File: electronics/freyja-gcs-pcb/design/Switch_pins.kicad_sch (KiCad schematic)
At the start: 21 parts, among them SW3 TS1210CJ 250GF 009, U3 ST-0-102-A01-T000-LF+PJ, U4 ST-0-102-A01-T000-LF+PJ, U5 ST-0-102-A01-T000-LF+PJ, U6 ST-0-102-A01-T000-LF+PJ, U7 ST-0-102-A01-T000-LF+PJ, U8 ST-0-102-A01-T000-LF+PJ

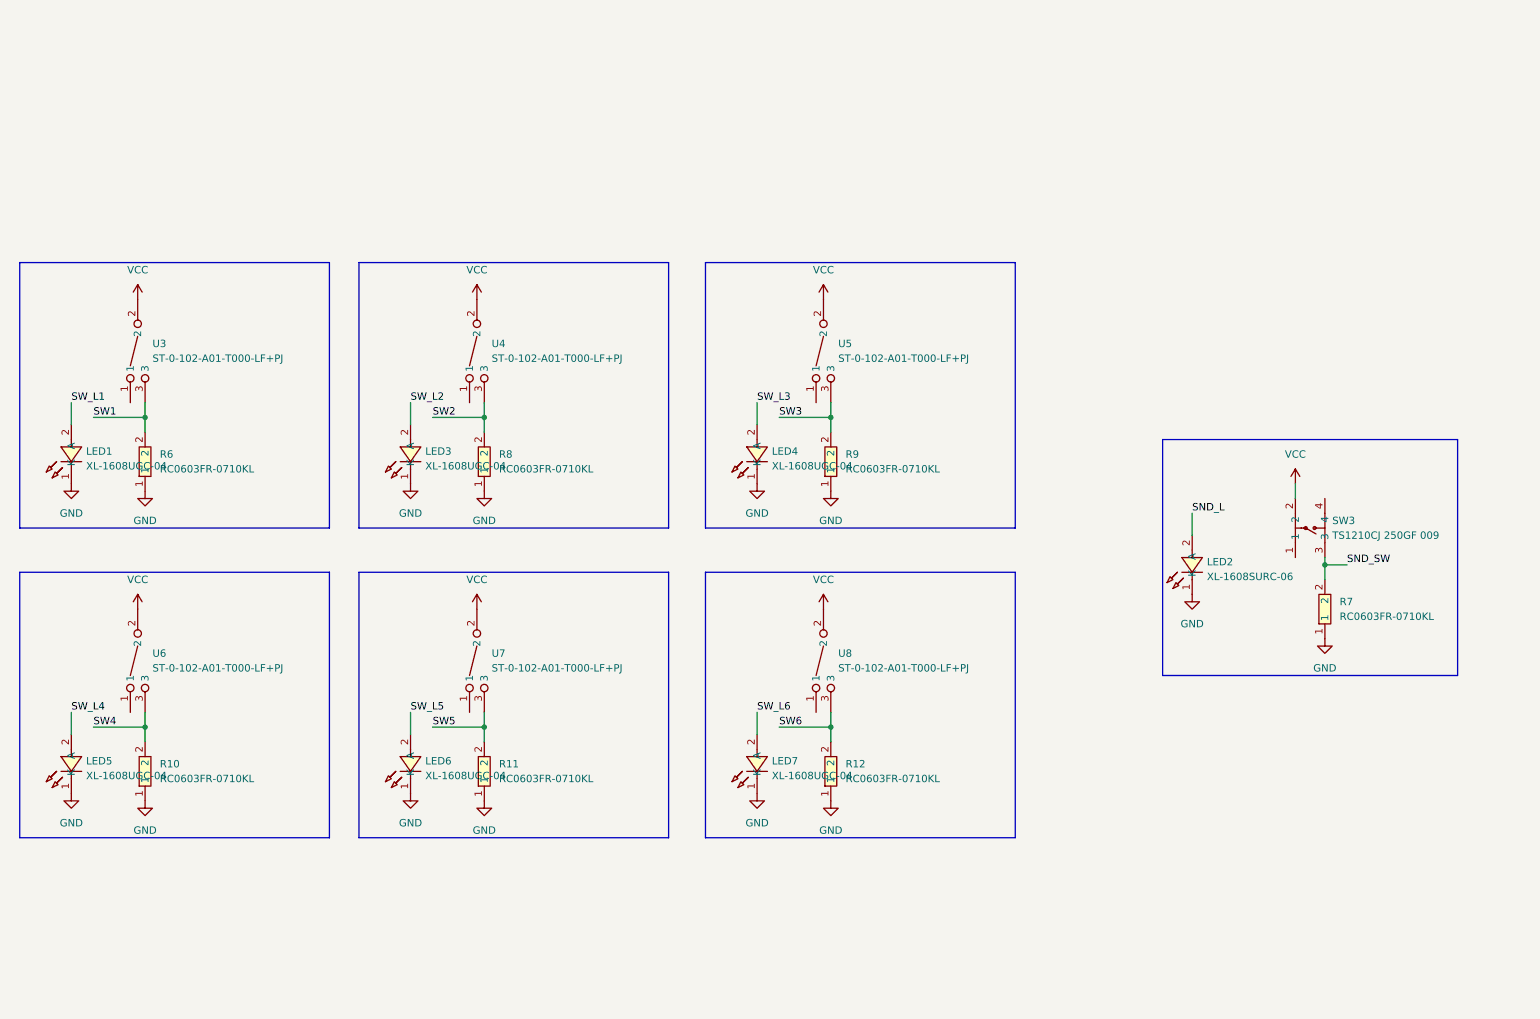
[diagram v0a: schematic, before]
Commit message: reset annotation
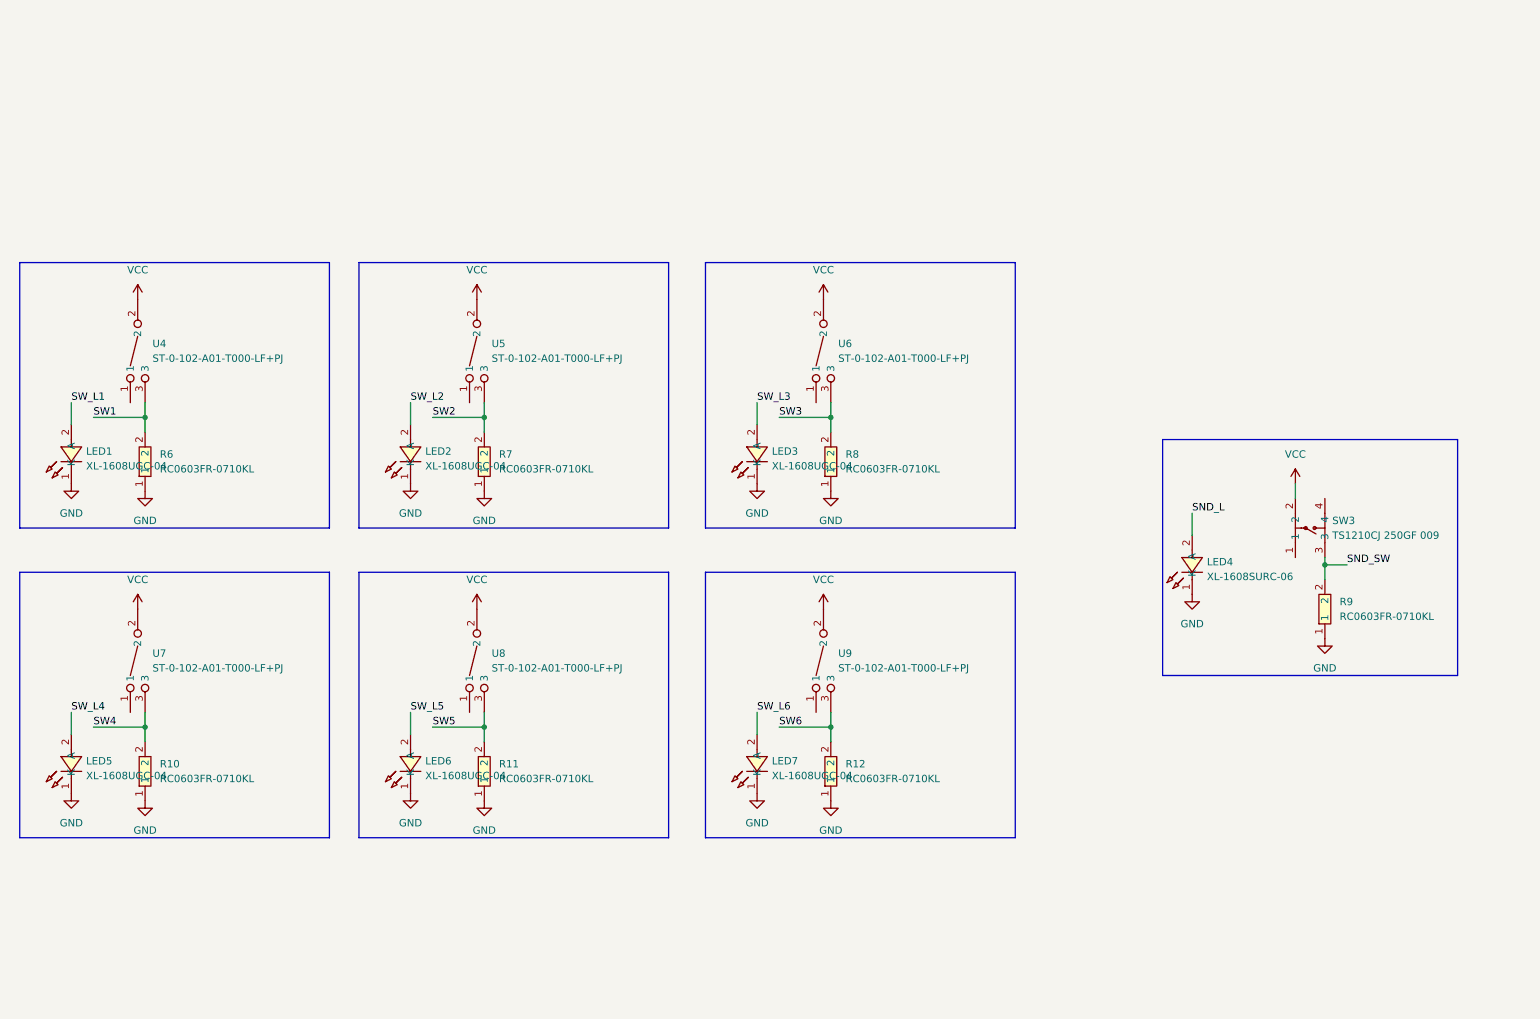
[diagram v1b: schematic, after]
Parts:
- renumbered LED3 to LED2, LED4 to LED3, LED2 to LED4, R8 to R7, R9 to R8, R7 to R9, U3 to U4, U4 to U5, U5 to U6, U6 to U7, U7 to U8, U8 to U9

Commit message: add led backlight driver
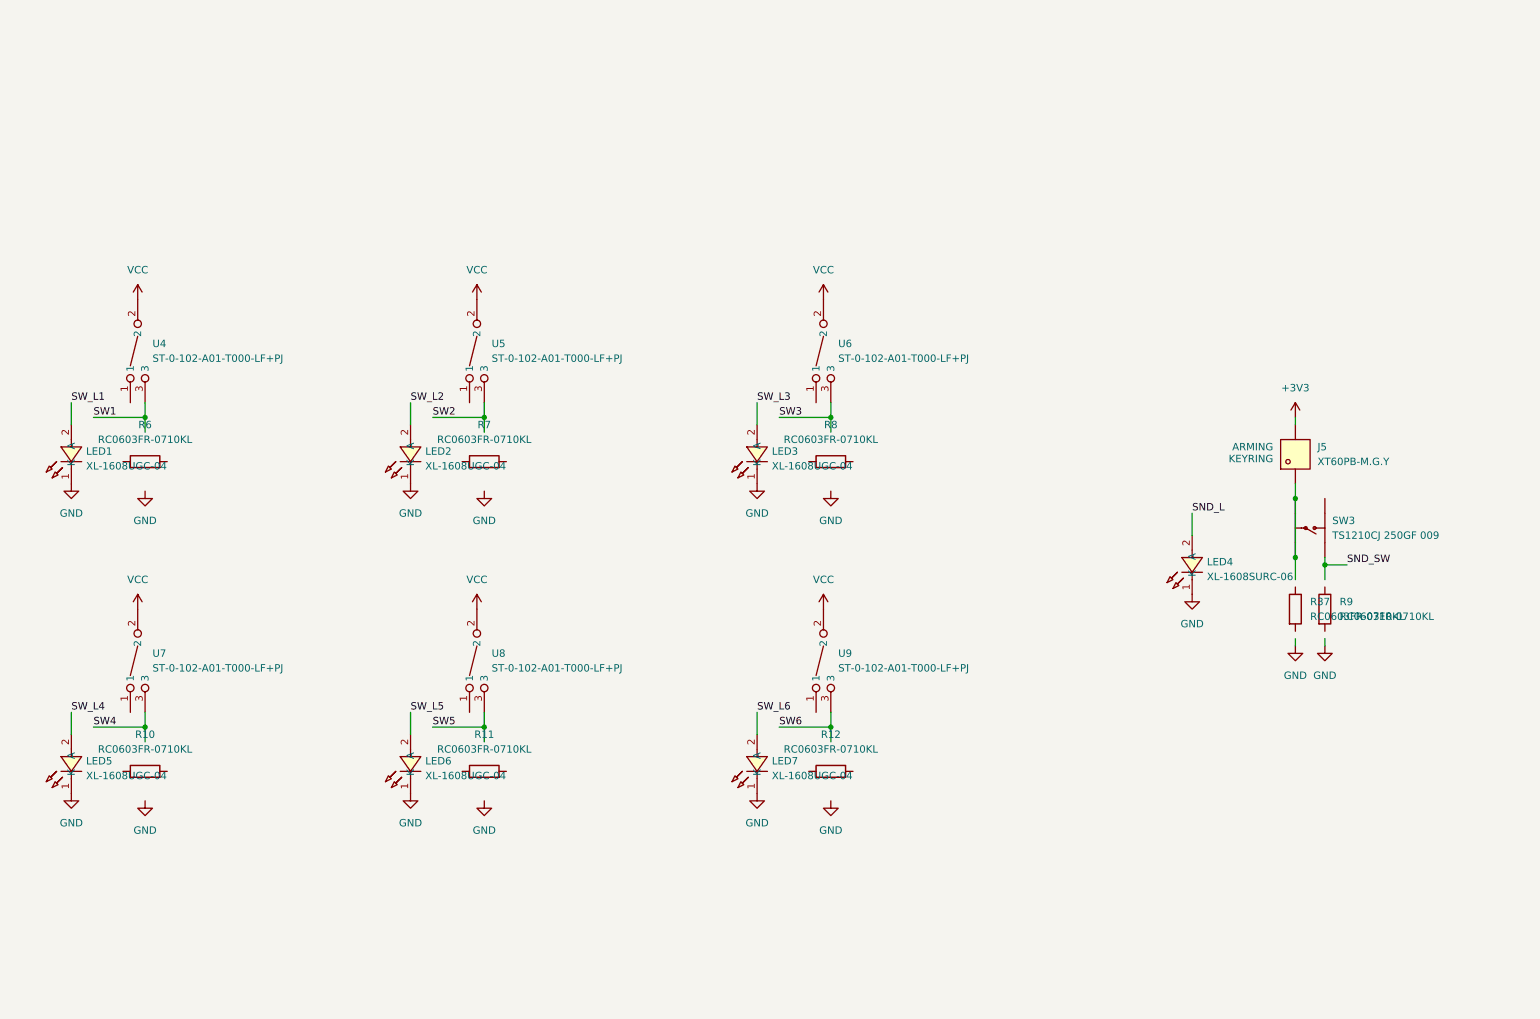
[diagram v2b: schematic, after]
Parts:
- added J5: XT60PB-M.G.Y, EasyEDA:CONN-TH_XT60PB-M, symbol EasyEDA:XT60PB-M.G.Y
- added R37: RC0603FR-0710KL, EasyEDA:R0603, symbol Device:R
- R10, R11, R12, R6, R7, R8, R9: symbol EasyEDA:RC0603FR-0710KL -> Device:R
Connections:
- net GND: no longer R10.1, R11.1, R12.1, R6.1, R7.1, R8.1, R9.1
- net SND_SW: no longer R9.2
- net SW1: no longer R6.2
- net SW2: no longer R7.2
- net SW3: no longer R8.2
- net SW4: no longer R10.2
- net SW5: no longer R11.2
- net SW6: no longer R12.2
- net VCC: no longer SW3.2
- net at SW3.1: now also SW3.2, J5.1
- new net +3V3: J5.2
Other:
- note added: "ARMING KEYRING"

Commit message: buttons and indicators
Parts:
- removed LED1, LED2, LED3, LED5, LED6, LED7: XL-1608UGC-04, EasyEDA:LED0603-RD_GREEN, symbol EasyEDA:XL-1608UGC-04
- removed LED4: XL-1608SURC-06, EasyEDA:LED0603-RD_RED, symbol EasyEDA:XL-1608SURC-06
- removed SW3: TS1210CJ 250GF 009, EasyEDA:SW-TH_4P-L12.0-W12.0-P5.00-LS12.5_TC-1103XX, symbol EasyEDA:TS1210CJ250GF009
- removed U5, U6, U7, U8, U9: ST-0-102-A01-T000-LF+PJ, EasyEDA:SW-TH_3P-L8.3-W5.2-P2.54_ST-0-102-A01-T000, symbol EasyEDA:ST-0-102-A01-T000-LF+PJ
- added D25, D27, D29, D32, D33, D34, D35, D43, D44, D45, D49: Green, EasyEDA:LED-TH_BD5.9-P2.54-RD_GREEN, symbol Device:LED
- added D26, D28, D30, D31, D36, D37, D38, D39, D40, D41, D42: 0603ESDA-05N, Diode_SMD:D_0603_1608Metric_Pad1.05x0.95mm_HandSolder, symbol Device:D_TVS
- added D46: Red, EasyEDA:LED-TH_BD5.9-P2.54-RD_GREEN, symbol Device:LED
- added D47, D48, D50: Yellow, EasyEDA:LED-TH_BD5.9-P2.54-RD_GREEN, symbol Device:LED
- added J100: XT60PB-F.G.Y, EasyEDA:CONN-TH_XT60PB-M, symbol EasyEDA:XT60PB-M.G.Y
- added Q11, Q12, Q13, Q14, Q15, Q16, Q17, Q18, Q19, Q20, Q21, Q22, Q23, Q24, Q25: NPN, EasyEDA:SOT-416_L1.6-W0.8-P1.00-LS1.6-BR, symbol EasyEDA:DTC043ZEBTL
- added R54, R55, R60, R61, R62, R63, R64, R65, R70: 10k, EasyEDA:R0603, symbol Device:R
- added R56, R57, R58, R59, R67, R71, R73: 120, symbol Device:R
- added R66, R68, R69, R72: 220, symbol Device:R
- added SW11, SW13, SW3: PB22E09071, EasyEDA:SW-TH_6P-L8.5-W8.5-P2.54-LS5.5, symbol EasyEDA:PB22E09071
- added SW12, SW4, SW5, SW6, SW7, SW8, SW9: ST-0-102-A01-T000-LF+PJ, EasyEDA:SW-TH_3P-L8.3-W5.2-P2.54_ST-0-102-A01-T000, symbol EasyEDA:ST-0-102-A01-T000-LF+PJ
- R10, R37, R6, R9: value RC0603FR-0710KL -> 10k
- R11, R12, R7, R8: value RC0603FR-0710KL -> 120; footprint EasyEDA:R0603 -> (none); LCSC Part C98220 -> (none)
- renumbered U4 to SW10
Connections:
- net SW1 is gone; now on net TGL0: SW10.3
- net VCC is gone; now on net +3V3: SW10.2
- net +3V3: now also J100.2, SW12.2, SW13.1, SW4.2, SW5.2, SW6.2, SW7.2, SW8.2, SW9.2
- net GND: now also R10.2, R37.1, R6.2, R9.2, D26.2 (A2), D28.2 (A2), D30.2 (A2), D31.2 (A2), D36.2 (A2), D37.2 (A2), D38.2 (A2), D39.2 (A2), D40.2 (A2), D41.2 (A2), D42.2 (A2), Q11.2 (E), Q12.2 (E), Q13.2 (E), Q14.2 (E), Q15.2 (E), Q16.2 (E), Q17.2 (E), Q18.2 (E), Q19.2 (E), Q20.2 (E), Q21.2 (E), Q22.2 (E), Q23.2 (E), Q24.2 (E), Q25.2 (E), R54.2, R55.2, R60.2, R61.2, R62.2, R63.2, R64.2, R65.1, R70.2, SW11.3, SW11.4, SW11.5, SW11.6, SW13.3, SW13.4, SW13.5, SW13.6, SW3.3, SW3.4, SW3.5, SW3.6
- net +5V: now reaches R8.1
- net +5V: now also R11.1, R12.1, R7.1, R56.1, R57.1, R58.1, R59.1, R66.1, R67.1, R68.1, R69.1, R71.1, R72.1, R73.1
- net at R8.2: now also D25.2 (A)
- net LAUNCH: now reaches R9.1
- net LAUNCH: now also D42.1 (A1), SW3.2
- net TGL0: now reaches R6.1
- net TGL0: now also D26.1 (A1)
- net CMD_ARMD: now reaches R37.2
- net CMD_ARMD: now also J5.1, SW11.1
- net at R12.2: now also D29.2 (A)
- net at R11.2: now also D27.2 (A)
- net at R7.2: now also D45.2 (A)
- net TGL1: now reaches R10.1
- net TGL1: now also D28.1 (A1), SW12.3
- new net: D43.1 (K), Q24.3 (C)
- new net: D50.2 (A), R66.2
- new net: D48.1 (K), Q12.3 (C)
- new net: D35.1 (K), Q19.3 (C)
- new net: D33.1 (K), Q23.3 (C)
- new net: D33.2 (A), R59.2
- new net: D25.1 (K), Q17.3 (C)
- new net: D29.1 (K), Q21.3 (C)
- new net: D50.1 (K), Q11.3 (C)
- new net: D48.2 (A), R72.2
- new net: D46.2 (A), R68.2
- new net: D47.1 (K), Q15.3 (C)
- new net: D47.2 (A), R69.2
- new net: D34.2 (A), R56.2
- new net: D34.1 (K), Q18.3 (C)
- new net: D49.1 (K), Q25.3 (C)
- new net: D32.1 (K), Q22.3 (C)
- new net: D43.2 (A), R71.2
- new net: D46.1 (K), Q14.3 (C)
- new net: D27.1 (K), Q20.3 (C)
- new net: D44.2 (A), R67.2
- new net: D44.1 (K), Q13.3 (C)
- new net: D32.2 (A), R58.2
- new net: D45.1 (K), Q16.3 (C)
- new net: D35.2 (A), R57.2
- new net: D49.2 (A), R73.2
- new net AUX_BTN: D39.1 (A1), R70.1, SW13.2
- new net AUX_LED: Q15.1 (B)
- new net CMD_ARMD_LED: Q11.1 (B)
- new net CMD_SEND: D41.1 (A1), R64.1, SW11.2
- new net CON_STS_LPD: Q24.1 (B)
- new net CON_STS_RKT: Q25.1 (B)
- new net FAULT_LED: Q14.1 (B)
- new net LAUNCHED_LED: Q13.1 (B)
- new net LAUNCH_ARMD: J100.1, R65.2, SW3.1
- new net LAUNCH_ARMD_LED: Q12.1 (B)
- new net TGL0_LED: Q16.1 (B)
- new net TGL1_LED: Q17.1 (B)
- new net TGL2: D30.1 (A1), R54.1, SW4.3
- new net TGL2_LED: Q20.1 (B)
- new net TGL3: D31.1 (A1), R55.1, SW5.3
- new net TGL3_LED: Q21.1 (B)
- new net TGL4: D37.1 (A1), R60.1, SW6.3
- new net TGL4_LED: Q18.1 (B)
- new net TGL5: D36.1 (A1), R61.1, SW7.3
- new net TGL5_LED: Q19.1 (B)
- new net TGL6: D38.1 (A1), R62.1, SW8.3
- new net TGL6_LED: Q22.1 (B)
- new net TGL7: D40.1 (A1), R63.1, SW9.3
- new net TGL7_LED: Q23.1 (B)
- no-connect marks 0 -> 8
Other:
- note added: "AUX BTN"
- note added: "COMMAND ARM KEYRING"
- note added: "COMMAND SEND BTN"
- note added: "LAUNCH ARM KEYRING"
- note added: "LAUNCH BTN"
- note removed: "ARMING KEYRING"
- moved on the sheet: J5, R6

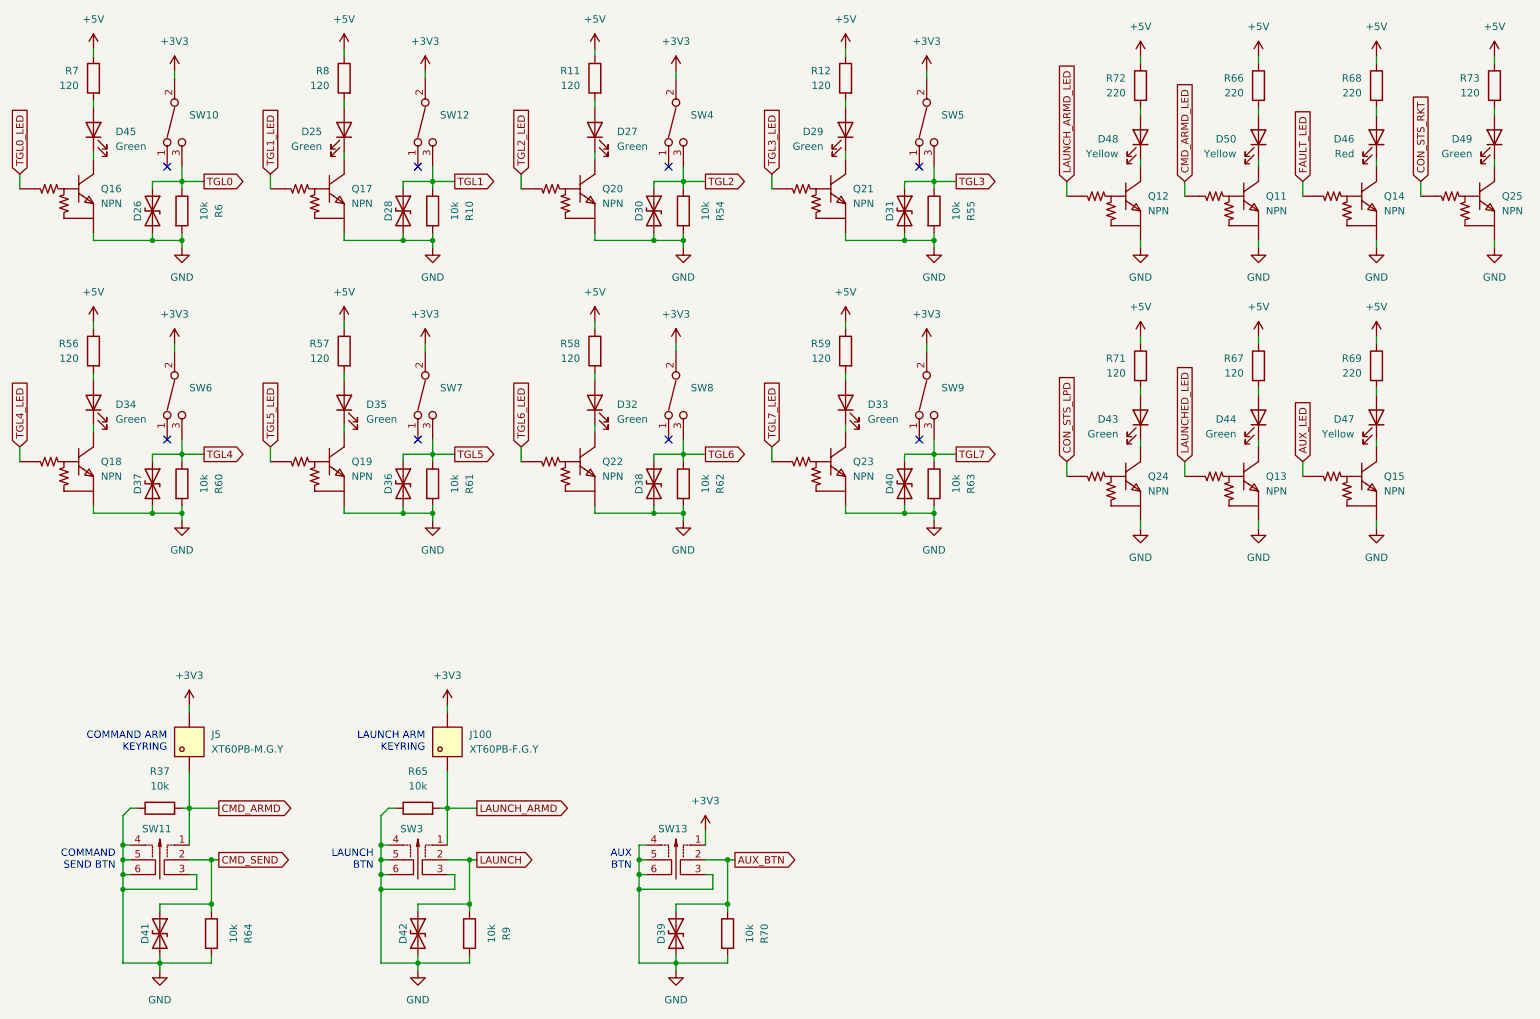
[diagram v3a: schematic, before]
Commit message: reset designators
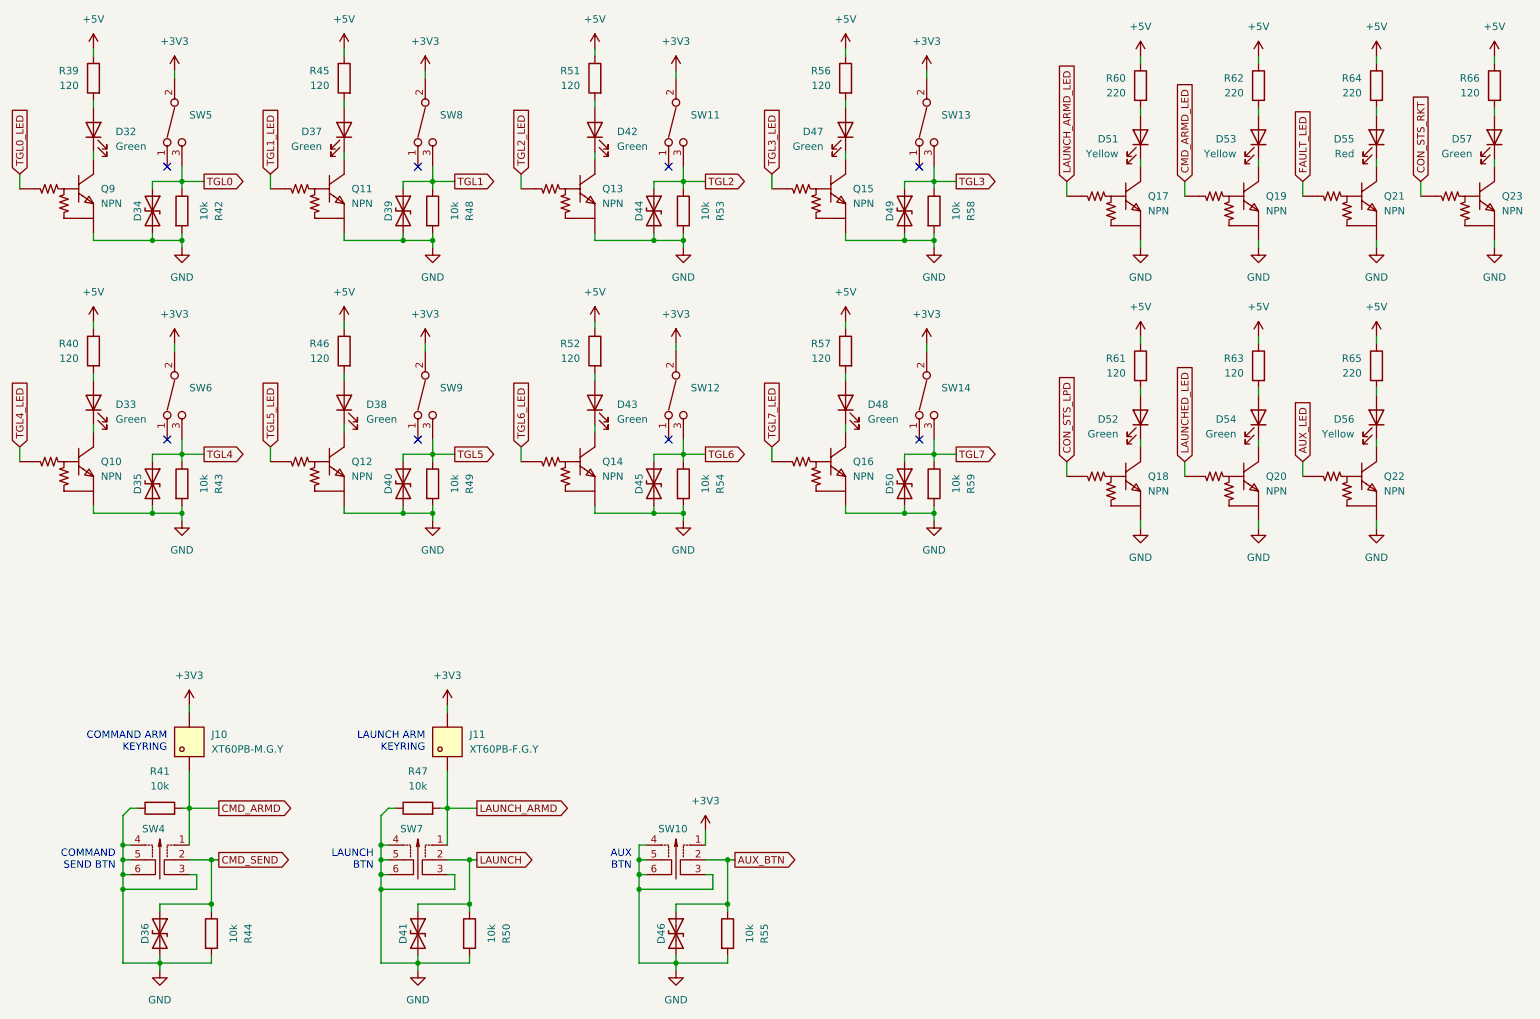
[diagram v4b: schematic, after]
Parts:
- renumbered D45 to D32, D34 to D33, D26 to D34, D37 to D35, D41 to D36, D25 to D37, D35 to D38, D28 to D39, D36 to D40, D42 to D41, D27 to D42, D32 to D43, D30 to D44, D38 to D45, D39 to D46, D29 to D47, D33 to D48, D31 to D49, D40 to D50, D48 to D51, D43 to D52, D50 to D53, D44 to D54, D46 to D55, D47 to D56, D49 to D57, J5 to J10, J100 to J11, Q18 to Q10, Q17 to Q11, Q19 to Q12, Q20 to Q13, Q22 to Q14, Q21 to Q15, Q23 to Q16, Q12 to Q17, Q24 to Q18, Q11 to Q19, Q13 to Q20, Q14 to Q21, Q15 to Q22, Q25 to Q23, Q16 to Q9, R7 to R39, R56 to R40, R37 to R41, R6 to R42, R60 to R43, R64 to R44, R8 to R45, R57 to R46, R65 to R47, R10 to R48, R61 to R49, R9 to R50, R11 to R51, R58 to R52, R54 to R53, R62 to R54, R70 to R55, R12 to R56, R59 to R57, R55 to R58, R63 to R59, R72 to R60, R71 to R61, R66 to R62, R67 to R63, R68 to R64, R69 to R65, R73 to R66, SW13 to SW10, SW4 to SW11, SW8 to SW12, SW5 to SW13, SW9 to SW14, SW11 to SW4, SW10 to SW5, SW3 to SW7, SW12 to SW8, SW7 to SW9
